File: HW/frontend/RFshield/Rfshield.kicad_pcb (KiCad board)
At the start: 4 copper layers, 73 x 50.9 mm, 332 parts, among them P10 TXENABLE, P11 RXENABLE, P12 XTAL2, P13 GCK1, P14 GCK2, P15 SGPIO_CLK, P16 DA0, P17 DA4, P18 DA7, P19 DD0, P2 VAA, P20 DD5, P21 DD9, P22 RSSI, P23 GND, P24 GND, P25 GND, P26 GND, P27 GND, P28 GND, P29 GND, P3 SCL, P30 GND, P31 GND, P32 GND, P33 XCVR_CLKOUT, P37 INTR, P38 CLKIN, P39 CLKOUT, P4 SDA, P5 SSP1_SCK, P6 SSP1_MOSI, P7 SSP1_MISO, P8 CS_XCVR, P9 CS_AD, Q1 MOSFET_P, T1 RX_BALUN, T2 TX_BALUN, U1 MAX2837, U2 MAX5864, U3 SI5351C, X1 GSG-XTAL4PIN

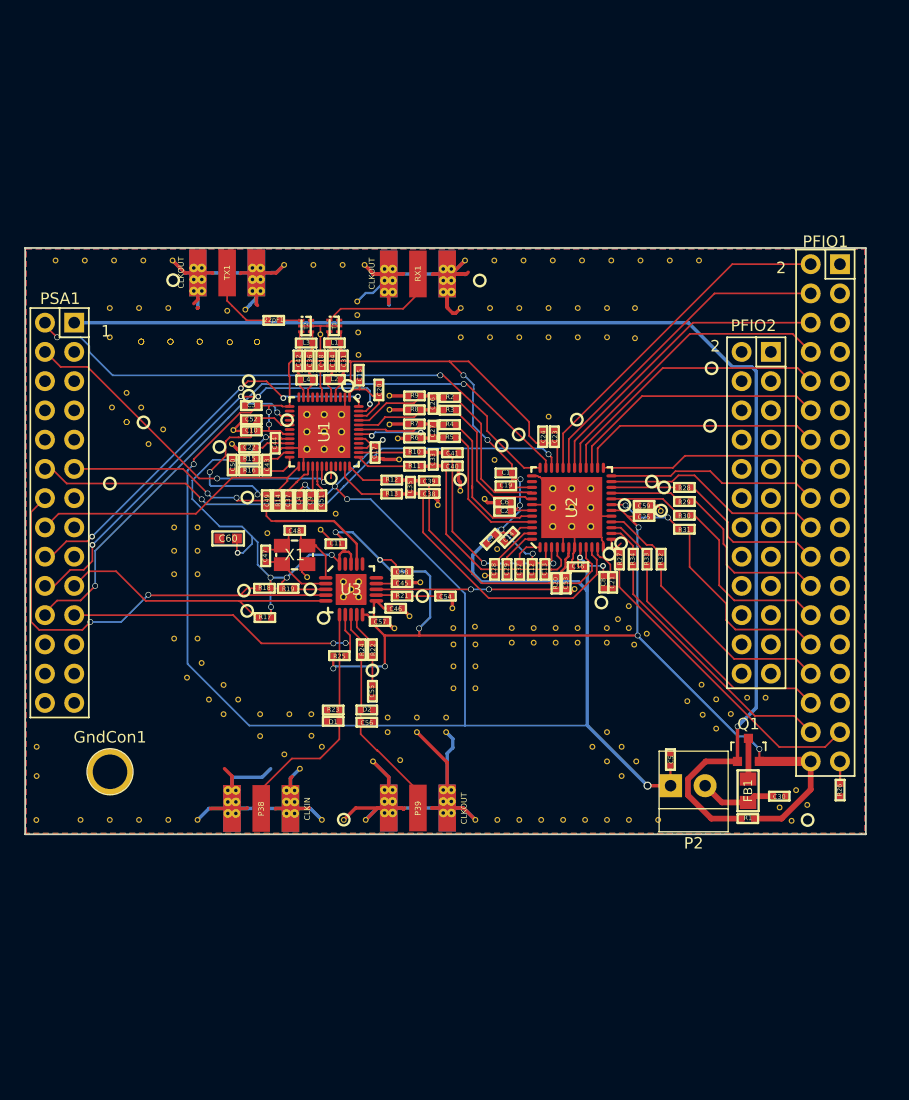
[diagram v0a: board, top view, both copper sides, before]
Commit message: shunt componnents grounded
ground vias placed in shunt components
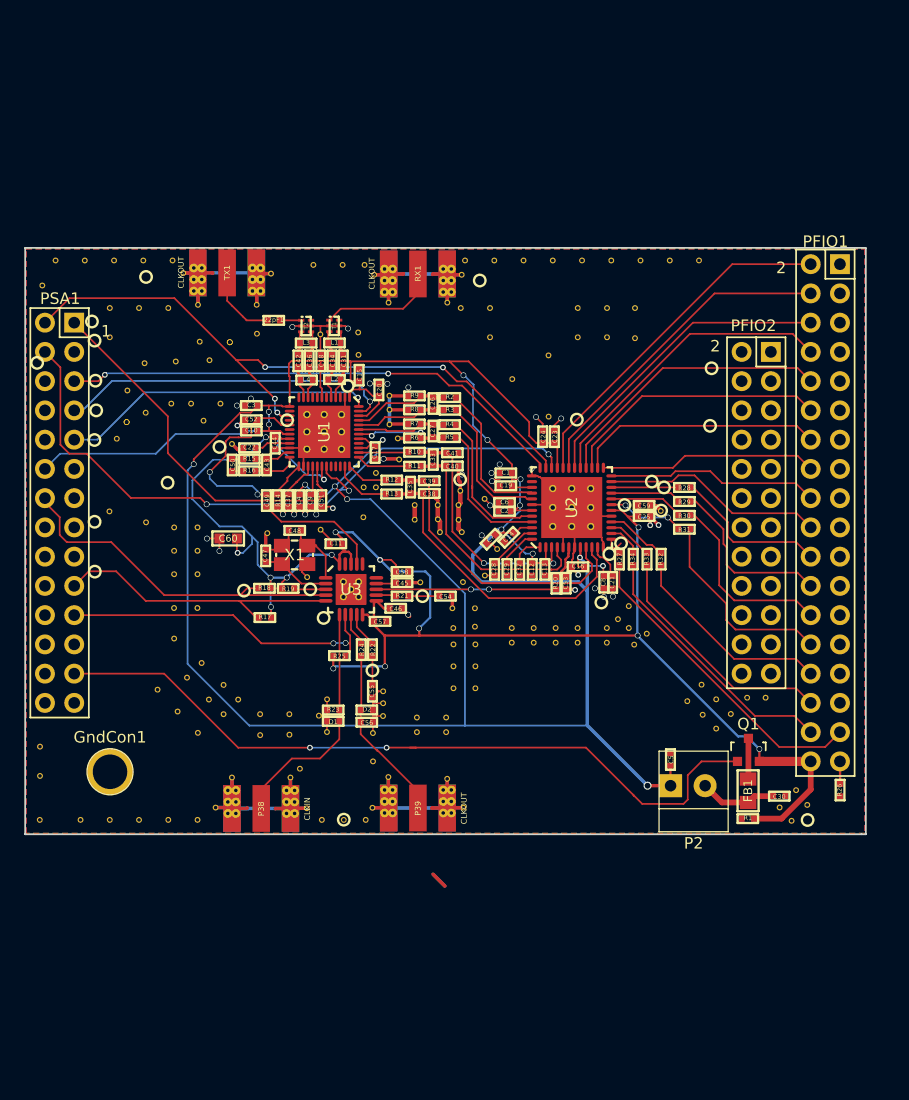
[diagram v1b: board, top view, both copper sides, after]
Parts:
- moved TH151 44.0 mm to (20.8, 69.6)
- moved TH20 38.8 mm to (49.8, 85.8)
- moved P5 37.7 mm to (25.3, 74.3)
- moved P9 35.7 mm to (25.4, 77.8)
- moved TH34 33.9 mm to (37.3, 112.3)
- moved TH2 30.9 mm to (55.1, 89.9)
- moved TH34 30.1 mm to (42.4, 112.3)
- moved TH34 28.9 mm to (55.3, 91.0)
- moved TH28 26.8 mm to (56.0, 71.0)
- moved TH33 26.1 mm to (57.0, 89.9)
- moved TH40 25.5 mm to (53.1, 88.6)
- moved TH3 24.5 mm to (35.9, 114.9)
- moved TH17 24.3 mm to (57.2, 91.0)
- moved TH17 24.2 mm to (32.2, 97.6)
- moved TH10 23.2 mm to (57.3, 95.3)
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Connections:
- PFIO1 pad 1: Net-(PFIO1-Pad1) -> (no net)
- PFIO1 pad 11: Net-(PFIO1-Pad11) -> (no net)
- PFIO1 pad 13: Net-(PFIO1-Pad13) -> (no net)
- PFIO1 pad 15: Net-(PFIO1-Pad15) -> (no net)
- PFIO1 pad 17: Net-(PFIO1-Pad17) -> (no net)
- PFIO1 pad 19: Net-(PFIO1-Pad19) -> (no net)
- PFIO1 pad 21: Net-(PFIO1-Pad21) -> (no net)
- PFIO1 pad 23: Net-(PFIO1-Pad23) -> (no net)
- PFIO1 pad 25: Net-(PFIO1-Pad25) -> (no net)
- PFIO1 pad 27: Net-(PFIO1-Pad27) -> (no net)
- PFIO1 pad 29: Net-(PFIO1-Pad29) -> (no net)
- PFIO1 pad 3: Net-(PFIO1-Pad3) -> (no net)
- PFIO1 pad 31: Net-(PFIO1-Pad31) -> (no net)
- PFIO1 pad 5: Net-(PFIO1-Pad5) -> (no net)
- PFIO1 pad 7: Net-(PFIO1-Pad7) -> (no net)
- PFIO1 pad 9: Net-(PFIO1-Pad9) -> (no net)
- PFIO2 pad 1: Net-(PFIO2-Pad1) -> (no net)
- PFIO2 pad 10: Net-(PFIO2-Pad10) -> (no net)
- PFIO2 pad 11: Net-(PFIO2-Pad11) -> (no net)
- PFIO2 pad 12: Net-(PFIO2-Pad12) -> (no net)
- PFIO2 pad 13: Net-(PFIO2-Pad13) -> (no net)
- PFIO2 pad 14: Net-(PFIO2-Pad14) -> (no net)
- PFIO2 pad 15: Net-(PFIO2-Pad15) -> (no net)
- PFIO2 pad 16: Net-(PFIO2-Pad16) -> (no net)
- PFIO2 pad 17: Net-(PFIO2-Pad17) -> (no net)
- PFIO2 pad 18: Net-(PFIO2-Pad18) -> (no net)
- PFIO2 pad 19: Net-(PFIO2-Pad19) -> (no net)
- PFIO2 pad 2: Net-(PFIO2-Pad2) -> (no net)
- PFIO2 pad 20: Net-(PFIO2-Pad20) -> (no net)
- PFIO2 pad 21: Net-(PFIO2-Pad21) -> (no net)
- PFIO2 pad 22: Net-(PFIO2-Pad22) -> (no net)
- PFIO2 pad 23: Net-(PFIO2-Pad23) -> (no net)
- PFIO2 pad 24: Net-(PFIO2-Pad24) -> (no net)
- PFIO2 pad 3: Net-(PFIO2-Pad3) -> (no net)
- PFIO2 pad 4: Net-(PFIO2-Pad4) -> (no net)
- PFIO2 pad 5: Net-(PFIO2-Pad5) -> (no net)
- PFIO2 pad 6: Net-(PFIO2-Pad6) -> (no net)
- PFIO2 pad 7: Net-(PFIO2-Pad7) -> (no net)
- PFIO2 pad 8: Net-(PFIO2-Pad8) -> (no net)
- PFIO2 pad 9: Net-(PFIO2-Pad9) -> (no net)
- PSA1 pad 1: !VAA_ENABLE -> SSP1_MISO
- PSA1 pad 10: Net-(PSA1-Pad10) -> (no net)
- PSA1 pad 11: SSP1_MISO -> XCVR_EN
- PSA1 pad 12: SSP1_MOSI -> CS_XCVR
- PSA1 pad 13: Net-(PSA1-Pad13) -> (no net)
- PSA1 pad 15: Net-(PSA1-Pad15) -> (no net)
- PSA1 pad 16: XCVR_EN -> (no net)
- PSA1 pad 17: Net-(PSA1-Pad17) -> (no net)
- PSA1 pad 18: RXENABLE -> (no net)
- PSA1 pad 2: CS_AD -> SSP1_SCK
- PSA1 pad 20: TXENABLE -> (no net)
- PSA1 pad 22: SSP1_SCK -> (no net)
- PSA1 pad 23: Net-(PSA1-Pad23) -> (no net)
- PSA1 pad 24: Net-(PSA1-Pad24) -> (no net)
- PSA1 pad 25: Net-(PSA1-Pad25) -> !VAA_ENABLE
- PSA1 pad 26: Net-(PSA1-Pad26) -> (no net)
- PSA1 pad 27: Net-(PSA1-Pad27) -> (no net)
- PSA1 pad 28: Net-(PSA1-Pad28) -> (no net)
- PSA1 pad 3: Net-(PSA1-Pad3) -> (no net)
- PSA1 pad 4: CS_XCVR -> SSP1_MOSI
- PSA1 pad 5: Net-(PSA1-Pad5) -> CS_AD
- PSA1 pad 6: Net-(PSA1-Pad6) -> (no net)
- PSA1 pad 7: Net-(PSA1-Pad7) -> TXENABLE
- PSA1 pad 8: Net-(PSA1-Pad8) -> (no net)
- PSA1 pad 9: Net-(PSA1-Pad9) -> RXENABLE
- U1 pad 12: Net-(U1-Pad12) -> (no net)
- U1 pad 14: Net-(U1-Pad14) -> (no net)
- U1 pad 18: Net-(U1-Pad18) -> (no net)
- U1 pad 3: Net-(U1-Pad3) -> (no net)
- U1 pad 33: Net-(U1-Pad33) -> (no net)
- U1 pad 34: Net-(U1-Pad34) -> (no net)
- U1 pad 40: Net-(U1-Pad40) -> (no net)
- U1 pad 6: Net-(U1-Pad6) -> (no net)
- U1 pad 8: Net-(U1-Pad8) -> (no net)
- U1 pad 9: Net-(U1-Pad9) -> (no net)
- U2 pad 38: Net-(U2-Pad38) -> (no net)
- U3 pad 15: MCU_CLK -> (no net)
- U3 pad 16: CLK6 -> (no net)
- U3 pad 19: MIX_CLK -> (no net)
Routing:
- net !VAA_ENABLE: track 107.8 -> 65.7 mm, vias 1 -> 2
- net XCVR_EN: track 26.2 -> 3.30 mm
- net SSP1_MOSI: track 48.5 -> 61.1 mm, vias 2 -> 3
- net GND: track 241.3 -> 230.3 mm, vias 0 -> 33
- net TXENABLE: track 39.4 -> 29.4 mm, vias 4 -> 1
- net SCL: track 40.7 -> 31.3 mm, vias 2 -> 0
- net RXENABLE: track 35.7 -> 27.3 mm, vias 4 -> 1
- net SSP1_MISO: track 25.8 -> 33.3 mm, vias 2 -> 0
- net (no net): track 0.17 -> 5.91 mm
- net CS_AD: track 49.3 -> 44.4 mm
- net SSP1_SCK: track 61.6 -> 58.3 mm, vias 3 -> 4
- net RSSI: track 1.03 -> 0.00 mm
- net CS_XCVR: track 30.4 -> 29.7 mm, vias 2 -> 1

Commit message: low budget version of rfshield netlisted
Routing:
- net (no net): track 5.91 -> 2.99 mm
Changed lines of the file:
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@@
     (thickness 1.6)
     (drawings 10)
-    (tracks 1254)
+    (tracks 1252)
     (zones 0)
     (modules 332)
@@
   (segment (start 21.03 93.11) (end 21.56 93.11) (width 0.15) (layer F.Cu) (net 0))
   (segment (start 21.03 93.11) (end 21.67 93.11) (width 0.15) (layer F.Cu) (net 0))
-  (segment (start 54.728 120.688) (end 55.76 121.72) (width 0.3) (layer F.Cu) (net 0))
-  (segment (start 54.728 120.688) (end 55.76 121.72) (width 0.3) (layer B.Cu) (net 0))
   (segment (start 24.12 90.02) (end 23.57 90.57) (width 0.15) (layer F.Cu) (net 0))
   (segment (start 50.6634 98.73) (end 50.8934 98.73) (width 0.3) (layer F.Cu) (net 1) (status C00000))

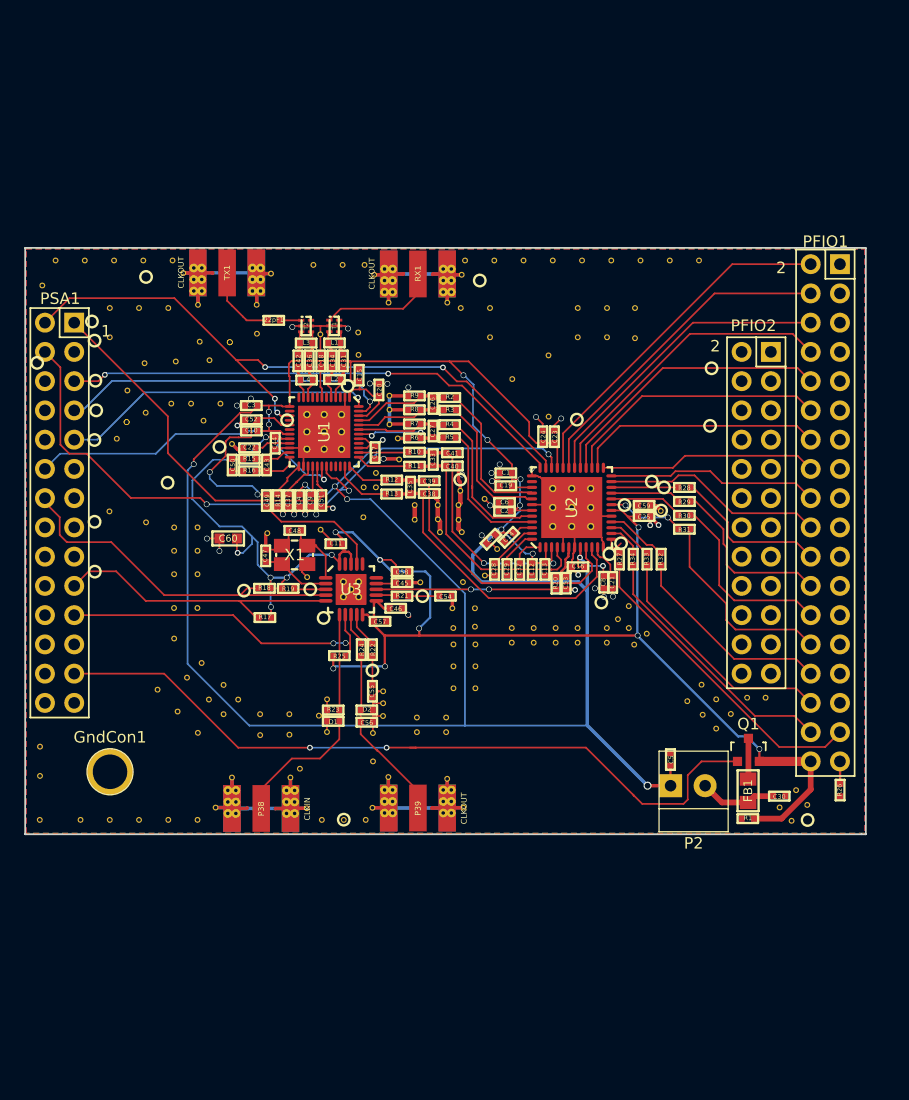
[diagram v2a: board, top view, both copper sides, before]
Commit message: smd discrete components switched to 0402 package
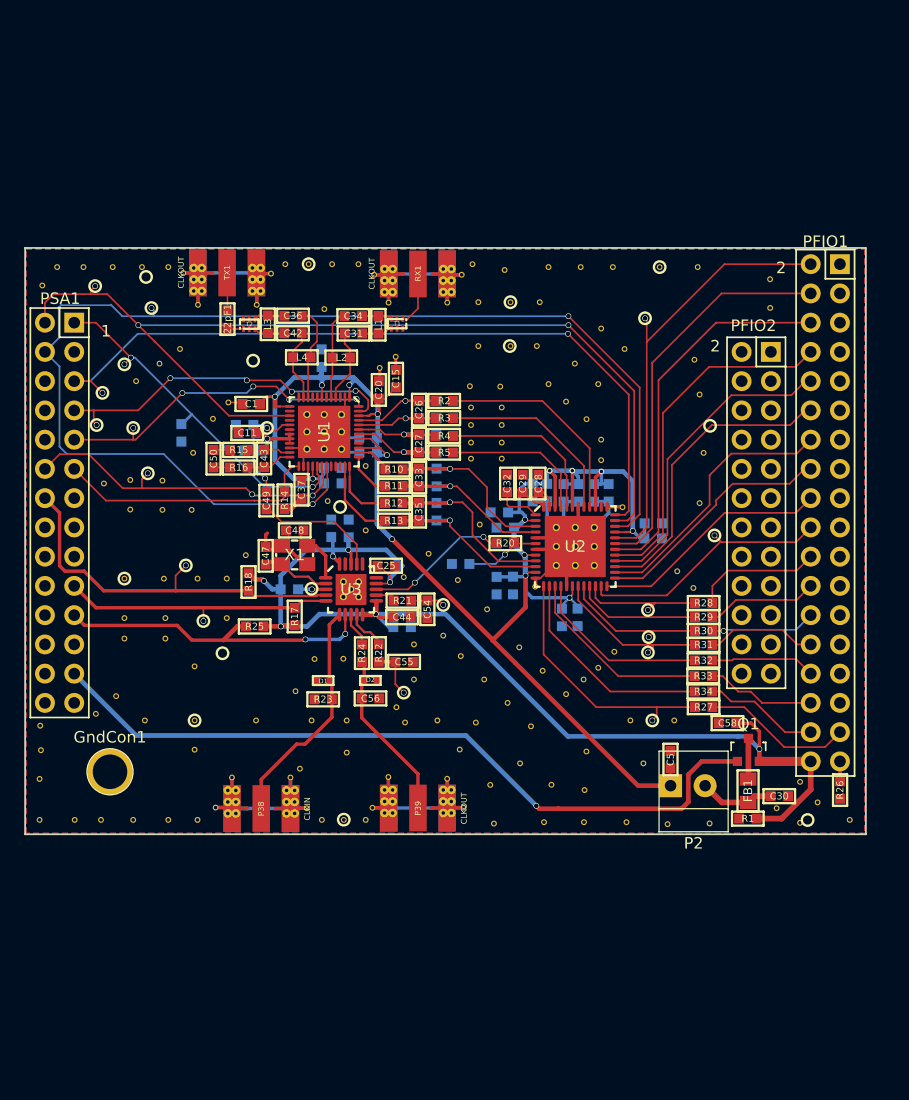
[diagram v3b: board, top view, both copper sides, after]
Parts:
- removed the TH1 at (56.4, 97.6)
- removed the TH17 at (26.7, 74.1)
- removed the TH18 at (61.6, 100.6)
- removed the TH18 at (78.0, 104.2)
- removed the TH18 at (79.3, 105.5)
- removed the TH18 at (80.6, 106.8)
- removed the TH18 at (34.6, 102.3)
- removed the TH18 at (78.2, 106.8)
- removed the TH18 at (82.0, 105.4)
- removed the TH18 at (83.6, 105.4)
- removed the TH26 at (34.8, 81.3)
- removed the TH28 at (29.8, 80.6)
- removed the TH28 at (28.1, 81.4)
- removed the TH28 at (28.2, 78.7)
- removed the TH28 at (27.3, 82.9)
- removed the TH28 at (29.7, 76.3)
- removed the TH34 at (58.4, 104.5)
- removed the TH34 at (56.5, 104.5)
- removed the TH34 at (58.4, 99.2)
- removed the TH34 at (58.4, 100.7)
- removed the TH34 at (56.5, 102.6)
- removed the TH40 at (33.7, 79.8)
- removed the TH41 at (36.3, 79.8)
- added TH18: CONN_1, opendous:1Pin_12mil_VIA, F.Cu at (44.4, 102.0)
- added TH18: CONN_1, opendous:1Pin_12mil_VIA, F.Cu at (75.9, 94.4)
- added TH18: CONN_1, opendous:1Pin_12mil_VIA, F.Cu at (70.5, 101.4)
- added TH18: CONN_1, opendous:1Pin_12mil_VIA, F.Cu at (48.9, 90.8)
- added TH18: CONN_1, opendous:1Pin_12mil_VIA, F.Cu at (67.8, 103.8)
- 22pF1, C1, C11, C15, C20, C25, C26, C27, C28, C29, C30, C31, C32, C33, C34, C35, C36, C37, C42, C43, C44, C47, C48, C49, C5, C50, C54, C55, C56, C58, L1, L2, L3, L4, R1, R10, R11, R12, R13, R14, R15, R16, R17, R18, R2, R20, R21, R22, R23, R24, R25, R26, R27, R28, R29, R3, R30, R31, R32, R33, R34, R4, R5: footprint hackrf1:GSG-0402 -> hackrf1:GSG-0603
- C10, C12, C13, C14, C16, C17, C18, C2, C21, C22, C23, C24, C3, C38, C39, C4, C40, C41, C45, C46, C51, C52, C53, C57, C59, C6, C7, C8, C9, R19, R6, R7, R8, R9: footprint hackrf1:GSG-0402 -> hackrf1:GSG-0603; moved to B.Cu
- C19: value 2.2uF -> 100nF; footprint hackrf1:GSG-0402 -> hackrf1:GSG-0603; moved to B.Cu
- C60: moved to B.Cu
- P10, P11, P12, P13, P14, P15, P16, P17, P18, P19, P20, P21, P22, P23, P24, P25, P26, P27, P28, P29, P3, P30, P31, P32, P33, P37, P4, P5, P6, P7, P8, P9: footprint kicadmos:GSG-TESTPOINT-30MIL-MASKONLY -> hackrf1:GSG-TESTPOINT-30MIL-MASKONLY
- moved TH28 69.7 mm to (90.9, 116.0)
- moved TH50 53.9 mm to (28.4, 89.0)
- moved TH151 52.8 mm to (27.2, 105.2)
- moved TH48 51.9 mm to (31.4, 95.0)
- moved TH18 46.9 mm to (25.4, 106.8)
- moved TH18 45.4 mm to (27.9, 100.2)
- moved TH18 43.9 mm to (27.9, 95.0)
- moved TH18 43.3 mm to (78.8, 116.3)
- moved TH13 42.3 mm to (67.9, 113.4)
- moved P28 42.2 mm to (27.9, 95.0)
- moved TH151 41.3 mm to (47.2, 110.1)
- moved TH18 41.1 mm to (31.2, 86.5)
- moved TH151 39.7 mm to (32.8, 75.1)
- moved TH43 36.9 mm to (28.4, 86.5)
- moved TH151 35.9 mm to (71.9, 107.3)
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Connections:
- C11 pad 1: VCC -> VAA
- C22 pad 1: VAA -> VCC
- C45 pad 1: VCC -> VAA
- C46 pad 1: VCC -> VAA
- C57 pad 1: VCC -> VAA
- U1 pad 16: /XCVR_CLKOUT -> (no net)
- U1 pad 20: VCC -> VAA
- U1 pad 32: RSSI -> (no net)
- U2 pad 18: VCC -> VAA
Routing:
- net VAA: track 249.5 -> 166.6 mm
- net GND: track 230.3 -> 162.6 mm, vias 33 -> 0
- net SSP1_MOSI: track 61.1 -> 109.4 mm
- net VCC: track 146.4 -> 104.1 mm, vias 14 -> 7
- net SSP1_SCK: track 58.3 -> 86.8 mm, vias 4 -> 3
- net CS_AD: track 44.4 -> 66.4 mm
- net DA0: track 2.37 -> 22.3 mm, vias 0 -> 1
- net XCVR_EN: track 3.30 -> 23.1 mm
- net DA1: track 3.13 -> 18.7 mm
- net Net-(PFIO1-Pad33): track 27.4 -> 13.1 mm
- net Net-(PFIO1-Pad34): track 23.0 -> 10.0 mm
- net DA2: track 4.03 -> 16.7 mm
- net /QA+: track 26.6 -> 14.7 mm, vias 0 -> 1
- net Net-(PFIO1-Pad32): track 21.1 -> 9.54 mm
- net DA3: track 5.46 -> 15.6 mm
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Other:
- net class Default: via_drill 0.3 -> 0.4

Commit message: ok
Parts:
- removed C9: 10nF, hackrf1:GSG-0603
- removed TH1 (x2), TH10, TH11, TH111, TH12, TH121, TH13 (x7), TH131, TH14, TH141, TH15, TH151 (x9), TH16, TH17 (x7), TH18 (x35), TH19, TH2, TH20, TH21, TH22, TH23 (x11), TH24, TH25 (x5), TH26, TH27, TH28 (x6), TH29, TH3, TH30 (x2), TH33, TH34 (x20), TH35, TH38, TH39, TH4, TH40 (x8), TH41 (x11), TH42, TH43, TH44, TH45 (x3), TH46, TH47, TH48, TH49, TH5, TH50, TH6, TH7, TH8, TH9: CONN_1, opendous:1Pin_12mil_VIA
- removed U3: SI5351C, hackrf1:GSG-QFN20-4
- moved C18 28.4 mm to (20.6, 61.5)
- moved P30 22.3 mm to (21.6, 68.1)
- moved P22 20.3 mm to (26.4, 89.9)
- moved P12 15.1 mm to (25.9, 86.4)
- moved P33 11.9 mm to (27.4, 73.7)
- moved C51 9.38 mm to (32.0, 91.7)
- moved C1 7.73 mm to (31.3, 81.1)
- moved C11 7.73 mm to (31.0, 83.6)
- moved C43 7.73 mm to (32.4, 85.8)
- moved C50 7.73 mm to (28.1, 85.9)
- moved C45 7.73 mm to (31.5, 85.2)
- moved R16 7.73 mm to (30.2, 86.6)
- moved C52 7.73 mm to (30.8, 82.9)
- moved R15 7.73 mm to (30.2, 85.1)
- moved R14 6.71 mm to (36.0, 91.5)
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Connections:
- C57 pad 1: VAA -> VCC
- PFIO1 pad 1: (no net) -> Net-(PFIO1-Pad1)
- PFIO1 pad 11: (no net) -> Net-(PFIO1-Pad11)
- PFIO1 pad 13: (no net) -> Net-(PFIO1-Pad13)
- PFIO1 pad 15: (no net) -> Net-(PFIO1-Pad15)
- PFIO1 pad 17: (no net) -> Net-(PFIO1-Pad17)
- PFIO1 pad 19: (no net) -> Net-(PFIO1-Pad19)
- PFIO1 pad 21: (no net) -> Net-(PFIO1-Pad21)
- PFIO1 pad 23: (no net) -> Net-(PFIO1-Pad23)
- PFIO1 pad 25: (no net) -> Net-(PFIO1-Pad25)
- PFIO1 pad 27: (no net) -> Net-(PFIO1-Pad27)
- PFIO1 pad 29: (no net) -> Net-(PFIO1-Pad29)
- PFIO1 pad 3: (no net) -> Net-(PFIO1-Pad3)
- PFIO1 pad 31: (no net) -> Net-(PFIO1-Pad31)
- PFIO1 pad 5: (no net) -> Net-(PFIO1-Pad5)
- PFIO1 pad 7: (no net) -> Net-(PFIO1-Pad7)
- PFIO1 pad 9: (no net) -> Net-(PFIO1-Pad9)
- PFIO2 pad 1: (no net) -> Net-(PFIO2-Pad1)
- PFIO2 pad 10: (no net) -> Net-(PFIO2-Pad10)
- PFIO2 pad 11: (no net) -> Net-(PFIO2-Pad11)
- PFIO2 pad 12: (no net) -> Net-(PFIO2-Pad12)
- PFIO2 pad 13: (no net) -> Net-(PFIO2-Pad13)
- PFIO2 pad 14: (no net) -> Net-(PFIO2-Pad14)
- PFIO2 pad 15: (no net) -> Net-(PFIO2-Pad15)
- PFIO2 pad 16: (no net) -> Net-(PFIO2-Pad16)
- PFIO2 pad 17: (no net) -> Net-(PFIO2-Pad17)
- PFIO2 pad 18: (no net) -> MIX_CLK
- PFIO2 pad 19: (no net) -> Net-(PFIO2-Pad19)
- PFIO2 pad 2: (no net) -> Net-(PFIO2-Pad2)
- PFIO2 pad 20: (no net) -> MCU_CLK
- PFIO2 pad 21: (no net) -> Net-(PFIO2-Pad21)
- PFIO2 pad 22: (no net) -> GCK2
- PFIO2 pad 23: (no net) -> Net-(PFIO2-Pad23)
- PFIO2 pad 24: (no net) -> SGPIO_CLK
- PFIO2 pad 3: (no net) -> Net-(PFIO2-Pad3)
- PFIO2 pad 4: (no net) -> Net-(PFIO2-Pad4)
- PFIO2 pad 5: (no net) -> Net-(PFIO2-Pad5)
- PFIO2 pad 6: (no net) -> Net-(PFIO2-Pad6)
- PFIO2 pad 7: (no net) -> Net-(PFIO2-Pad7)
- PFIO2 pad 8: (no net) -> Net-(PFIO2-Pad8)
- PFIO2 pad 9: (no net) -> Net-(PFIO2-Pad9)
- PSA1 pad 10: (no net) -> Net-(PSA1-Pad10)
- PSA1 pad 13: (no net) -> Net-(PSA1-Pad13)
- PSA1 pad 15: (no net) -> Net-(PSA1-Pad15)
- PSA1 pad 16: (no net) -> Net-(PSA1-Pad16)
- PSA1 pad 17: (no net) -> Net-(PSA1-Pad17)
- PSA1 pad 18: (no net) -> Net-(PSA1-Pad18)
- PSA1 pad 20: (no net) -> Net-(PSA1-Pad20)
- PSA1 pad 22: (no net) -> Net-(PSA1-Pad22)
- PSA1 pad 23: (no net) -> Net-(PSA1-Pad23)
- PSA1 pad 24: (no net) -> Net-(PSA1-Pad24)
- PSA1 pad 26: (no net) -> Net-(PSA1-Pad26)
- PSA1 pad 27: (no net) -> Net-(PSA1-Pad27)
- PSA1 pad 28: (no net) -> Net-(PSA1-Pad28)
- PSA1 pad 3: (no net) -> Net-(PSA1-Pad3)
- PSA1 pad 6: (no net) -> Net-(PSA1-Pad6)
- PSA1 pad 8: (no net) -> Net-(PSA1-Pad8)
- U1 pad 12: (no net) -> Net-(U1-Pad12)
- U1 pad 14: (no net) -> Net-(U1-Pad14)
- U1 pad 16: (no net) -> /XCVR_CLKOUT
- U1 pad 18: (no net) -> Net-(U1-Pad18)
- U1 pad 3: (no net) -> Net-(U1-Pad3)
- U1 pad 32: (no net) -> RSSI
- U1 pad 33: (no net) -> Net-(U1-Pad33)
- U1 pad 34: (no net) -> Net-(U1-Pad34)
- U1 pad 40: (no net) -> Net-(U1-Pad40)
- U1 pad 6: (no net) -> Net-(U1-Pad6)
- U1 pad 8: (no net) -> Net-(U1-Pad8)
- U1 pad 9: (no net) -> Net-(U1-Pad9)
- U2 pad 38: (no net) -> Net-(U2-Pad38)
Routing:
- net GND: track 162.6 -> 39.5 mm
- net SSP1_MOSI: track 109.4 -> 0.00 mm, vias 3 -> 0
- net SSP1_SCK: track 86.8 -> 0.00 mm, vias 3 -> 0
- net VCC: track 104.1 -> 19.1 mm, vias 7 -> 1
- net VAA: track 166.6 -> 83.9 mm, vias 16 -> 7
- net CS_AD: track 66.4 -> 0.00 mm, vias 2 -> 0
- net !VAA_ENABLE: track 65.6 -> 18.7 mm, vias 1 -> 0
- net SCL: track 34.0 -> 0.00 mm, vias 1 -> 0
- net TXENABLE: track 31.3 -> 0.00 mm, vias 5 -> 0
- net SSP1_MISO: track 31.2 -> 0.00 mm, vias 3 -> 0
- net CS_XCVR: track 30.3 -> 0.00 mm, vias 3 -> 0
- net OEB: track 28.8 -> 0.00 mm, vias 2 -> 0
- net RXENABLE: track 28.7 -> 0.00 mm, vias 5 -> 0
- net SDA: track 24.0 -> 0.00 mm, vias 1 -> 0
- net XCVR_EN: track 23.1 -> 0.00 mm
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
